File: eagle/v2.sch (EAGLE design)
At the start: 55 parts, among them IC1 MEGA8-AI

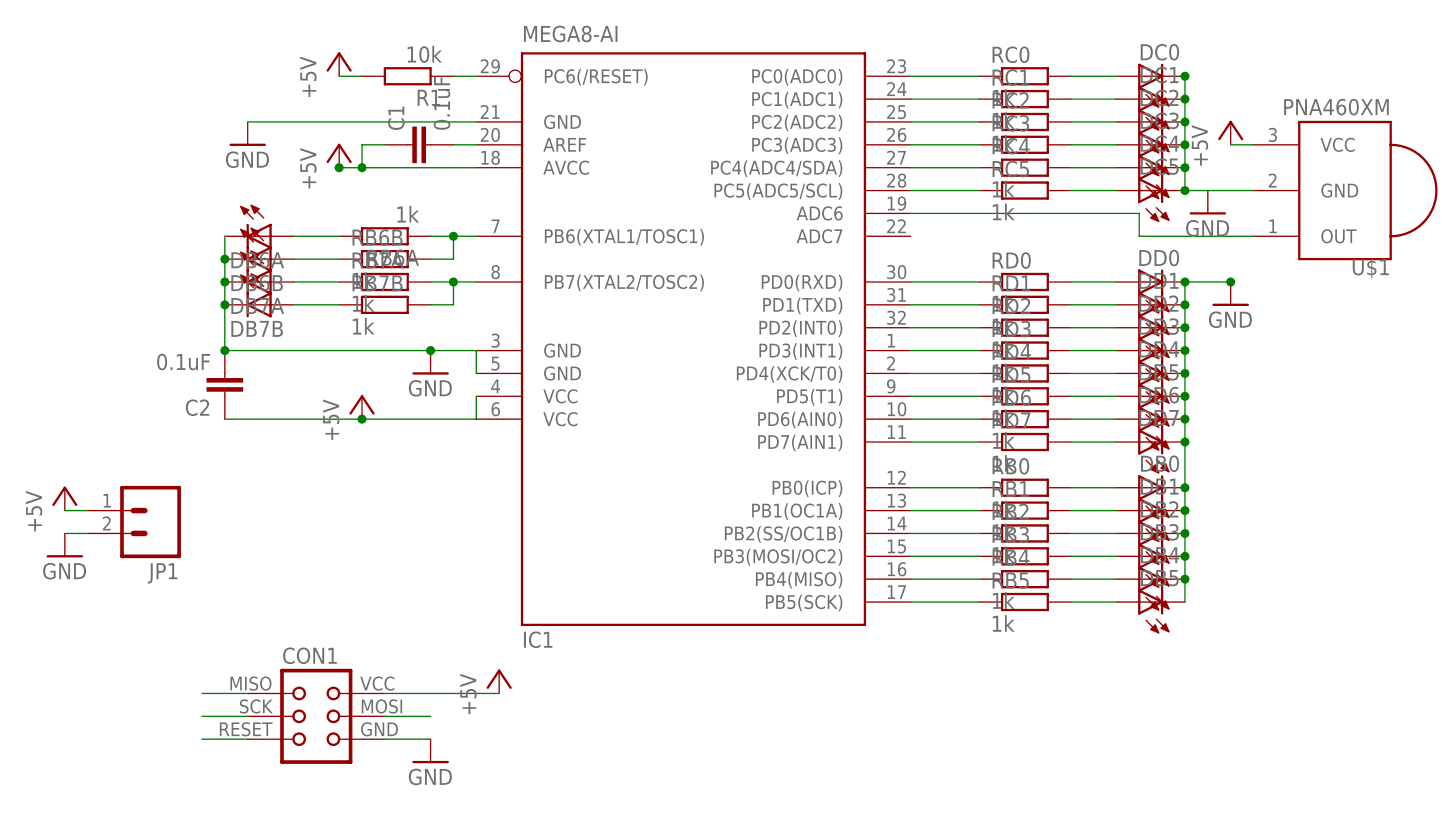
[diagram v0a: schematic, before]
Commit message: Update hierarchy
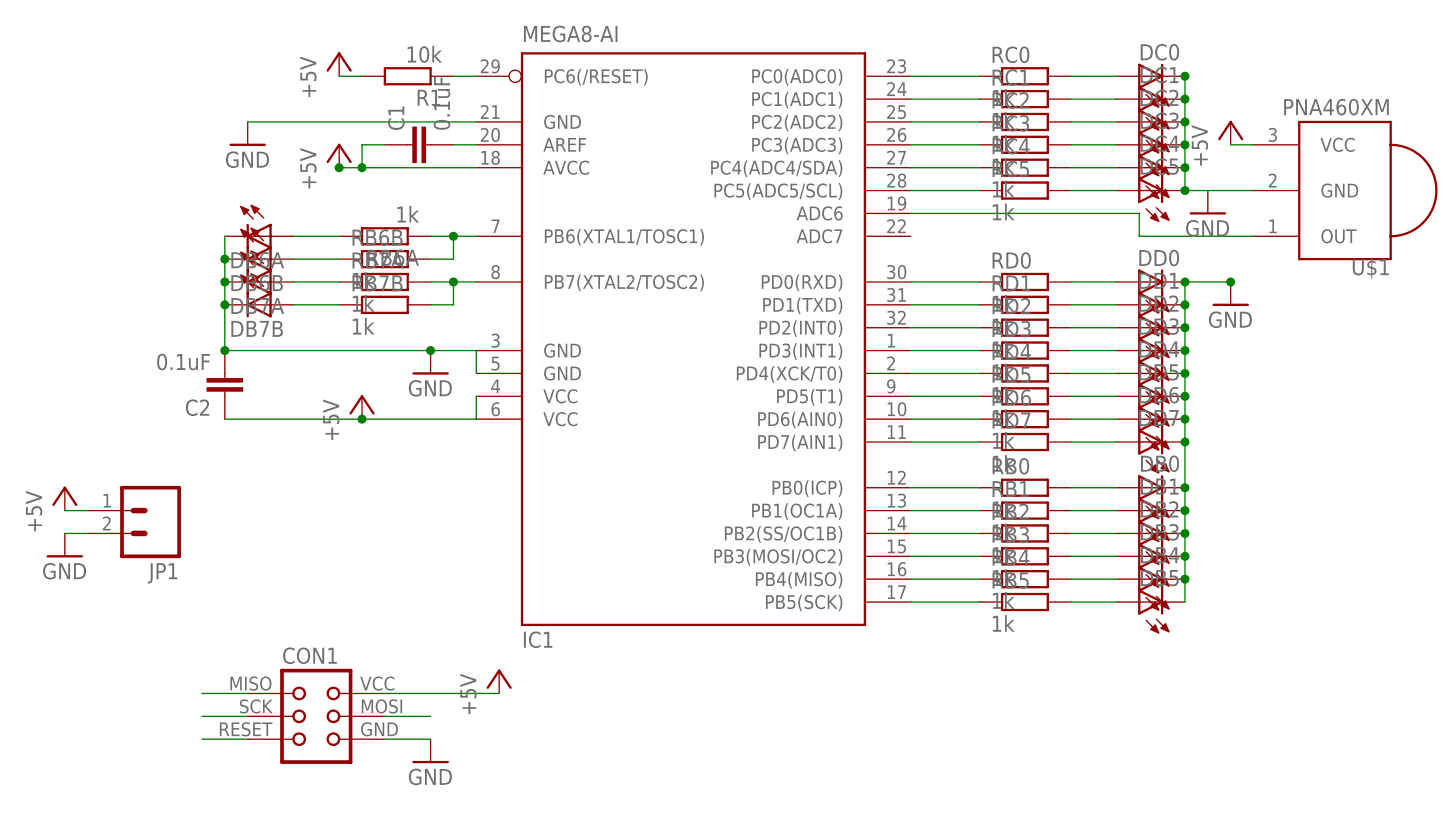
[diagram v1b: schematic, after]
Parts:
- RB3, RC3: value (none) -> 1k
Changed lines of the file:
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@@
 <class number="0" name="default" width="0" drill="0">
+</class>
+<class number="1" name="power" width="0.4064" drill="0">
 </class>
 </classes>
@@
 <part name="RC1" library="resistor" deviceset="R-EU_" device="M1206" value="1k"/>
 <part name="RC2" library="resistor" deviceset="R-EU_" device="M1206" value="1k"/>
-<part name="RC3" library="resistor" deviceset="R-EU_" device="M1206"/>
+<part name="RC3" library="resistor" deviceset="R-EU_" device="M1206" value="1k"/>
 <part name="RC4" library="resistor" deviceset="R-EU_" device="M1206" value="1k"/>
 <part name="RC5" library="resistor" deviceset="R-EU_" device="M1206" value="1k"/>
@@
 <part name="RB1" library="resistor" deviceset="R-EU_" device="M1206" value="1k"/>
 <part name="RB2" library="resistor" deviceset="R-EU_" device="M1206" value="1k"/>
-<part name="RB3" library="resistor" deviceset="R-EU_" device="M1206"/>
+<part name="RB3" library="resistor" deviceset="R-EU_" device="M1206" value="1k"/>
 <part name="RB4" library="resistor" deviceset="R-EU_" device="M1206" value="1k"/>
 <part name="RB6A" library="resistor" deviceset="R-EU_" device="M1206" value="1k"/>
@@
 </segment>
 </net>
-<net name="GND" class="0">
+<net name="GND" class="1">
 <segment>
 <pinref part="IC1" gate="G$1" pin="GND@2"/>
@@
 </segment>
 </net>
-<net name="+5V" class="0">
+<net name="+5V" class="1">
 <segment>
 <pinref part="IC1" gate="G$1" pin="VCC@2"/>
